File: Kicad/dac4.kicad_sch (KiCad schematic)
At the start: 10 parts

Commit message: Update schematic files to Kicad 6.
Had to fix some symbols which didn't have perfect matches in K6.
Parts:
- renumbered R1501 to R9001, R1502 to R9002, R1503 to R9003, R1504 to R9004, R1505 to R9005, R1506 to R9006, R1507 to R9007, R1508 to R9008, R1509 to R9009, R1510 to R9010
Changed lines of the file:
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@@
   (symbol (lib_id "Device:R") (at 88.9 68.58 0) (unit 1)
     (in_bom yes) (on_board yes)
-    (property "Reference" "R1501" (id 0) (at 90.678 67.4116 0)
+    (property "Reference" "R9001" (id 0) (at 90.678 67.4116 0)
       (effects (font (size 1.27 1.27)) (justify left))
     )
@@
   (symbol (lib_id "Device:R") (at 165.1 68.58 0) (unit 1)
     (in_bom yes) (on_board yes)
-    (property "Reference" "R1508" (id 0) (at 166.878 67.4116 0)
+    (property "Reference" "R9008" (id 0) (at 166.878 67.4116 0)
       (effects (font (size 1.27 1.27)) (justify left))
     )
@@
   (symbol (lib_id "Device:R") (at 101.6 76.2 270) (unit 1)
     (in_bom yes) (on_board yes)
-    (property "Reference" "R1503" (id 0) (at 101.6 78.74 90))
+    (property "Reference" "R9003" (id 0) (at 101.6 78.74 90))
     (property "Value" "12k" (id 1) (at 101.6 81.28 90))
     (property "Footprint" "Resistor_SMD:R_0805_2012Metric_Pad1.20x1.40mm_HandSolder" (id 2) (at 101.6 74.422 90)
@@
   (symbol (lib_id "Device:R") (at 114.3 68.58 0) (unit 1)
     (in_bom yes) (on_board yes)
-    (property "Reference" "R1504" (id 0) (at 116.078 67.4116 0)
+    (property "Reference" "R9004" (id 0) (at 116.078 67.4116 0)
       (effects (font (size 1.27 1.27)) (justify left))
     )
@@
   (symbol (lib_id "Device:R") (at 127 76.2 270) (unit 1)
     (in_bom yes) (on_board yes)
-    (property "Reference" "R1505" (id 0) (at 127 78.74 90))
+    (property "Reference" "R9005" (id 0) (at 127 78.74 90))
     (property "Value" "12k" (id 1) (at 127 81.28 90))
     (property "Footprint" "Resistor_SMD:R_0805_2012Metric_Pad1.20x1.40mm_HandSolder" (id 2) (at 127 74.422 90)
@@
   (symbol (lib_id "Device:R") (at 152.4 76.2 270) (unit 1)
     (in_bom yes) (on_board yes)
-    (property "Reference" "R1507" (id 0) (at 152.4 78.74 90))
+    (property "Reference" "R9007" (id 0) (at 152.4 78.74 90))
     (property "Value" "12k" (id 1) (at 152.4 81.28 90))
     (property "Footprint" "Resistor_SMD:R_0805_2012Metric_Pad1.20x1.40mm_HandSolder" (id 2) (at 152.4 74.422 90)
@@
   (symbol (lib_id "Device:R") (at 177.8 76.2 270) (unit 1)
     (in_bom yes) (on_board yes)
-    (property "Reference" "R1509" (id 0) (at 177.8 78.74 90))
+    (property "Reference" "R9009" (id 0) (at 177.8 78.74 90))
     (property "Value" "12k" (id 1) (at 177.8 81.28 90))
     (property "Footprint" "Resistor_SMD:R_0805_2012Metric_Pad1.20x1.40mm_HandSolder" (id 2) (at 177.8 74.422 90)
@@
   (symbol (lib_id "Device:R") (at 191.77 83.82 0) (unit 1)
     (in_bom yes) (on_board yes)
-    (property "Reference" "R1510" (id 0) (at 193.548 82.6516 0)
+    (property "Reference" "R9010" (id 0) (at 193.548 82.6516 0)
       (effects (font (size 1.27 1.27)) (justify left))
     )
@@
   (symbol (lib_id "power:GND") (at 88.9 91.44 0) (unit 1)
     (in_bom yes) (on_board yes)
-    (property "Reference" "#PWR01501" (id 0) (at 88.9 97.79 0)
+    (property "Reference" "#PWR09001" (id 0) (at 88.9 97.79 0)
       (effects (font (size 1.27 1.27)) hide)
     )
@@
   (symbol (lib_id "power:GND") (at 191.77 91.44 0) (unit 1)
     (in_bom yes) (on_board yes)
-    (property "Reference" "#PWR01502" (id 0) (at 191.77 97.79 0)
+    (property "Reference" "#PWR09002" (id 0) (at 191.77 97.79 0)
       (effects (font (size 1.27 1.27)) hide)
     )
@@
   (symbol (lib_id "Device:R") (at 88.9 83.82 0) (unit 1)
     (in_bom yes) (on_board yes)
-    (property "Reference" "R1502" (id 0) (at 90.678 82.6516 0)
+    (property "Reference" "R9002" (id 0) (at 90.678 82.6516 0)
       (effects (font (size 1.27 1.27)) (justify left))
     )
@@
   (symbol (lib_id "Device:R") (at 139.7 68.58 0) (unit 1)
     (in_bom yes) (on_board yes)
-    (property "Reference" "R1506" (id 0) (at 141.478 67.4116 0)
-      (effects (font (size 1.27 1.27)) (justify left))
-    )
+    (property "Reference" "R9006" (id 0) (at 141.478 67.4116 0)
+      (effects (font (size 1.27 1.27)) (justify left))
+    )

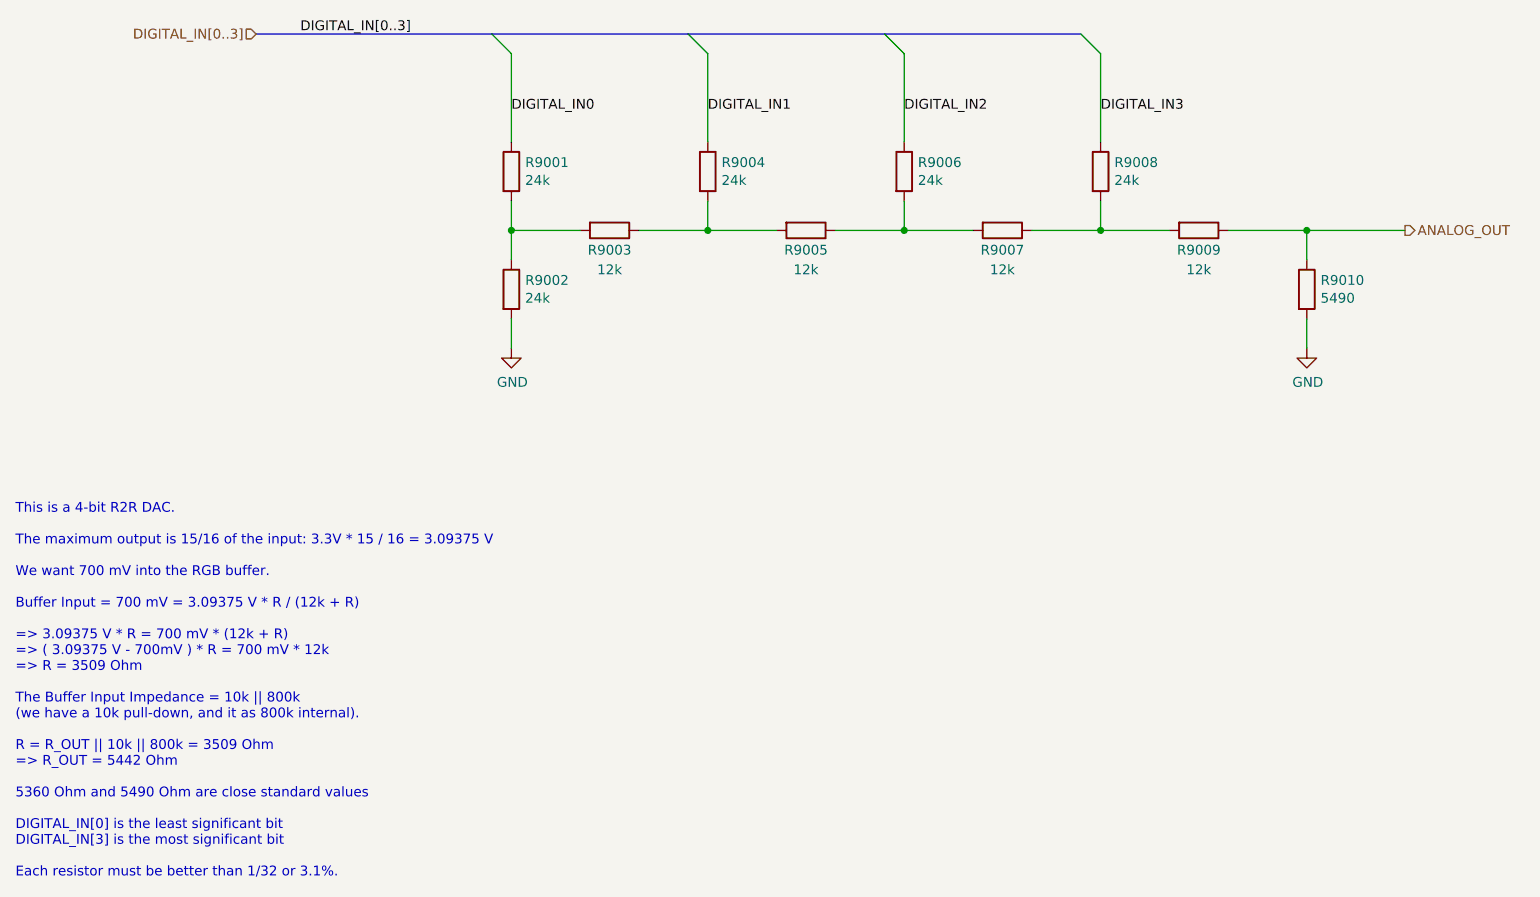
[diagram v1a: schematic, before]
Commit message: Imported sheets from Neotron Pico.
Standardised on +3V3 not +3.3V
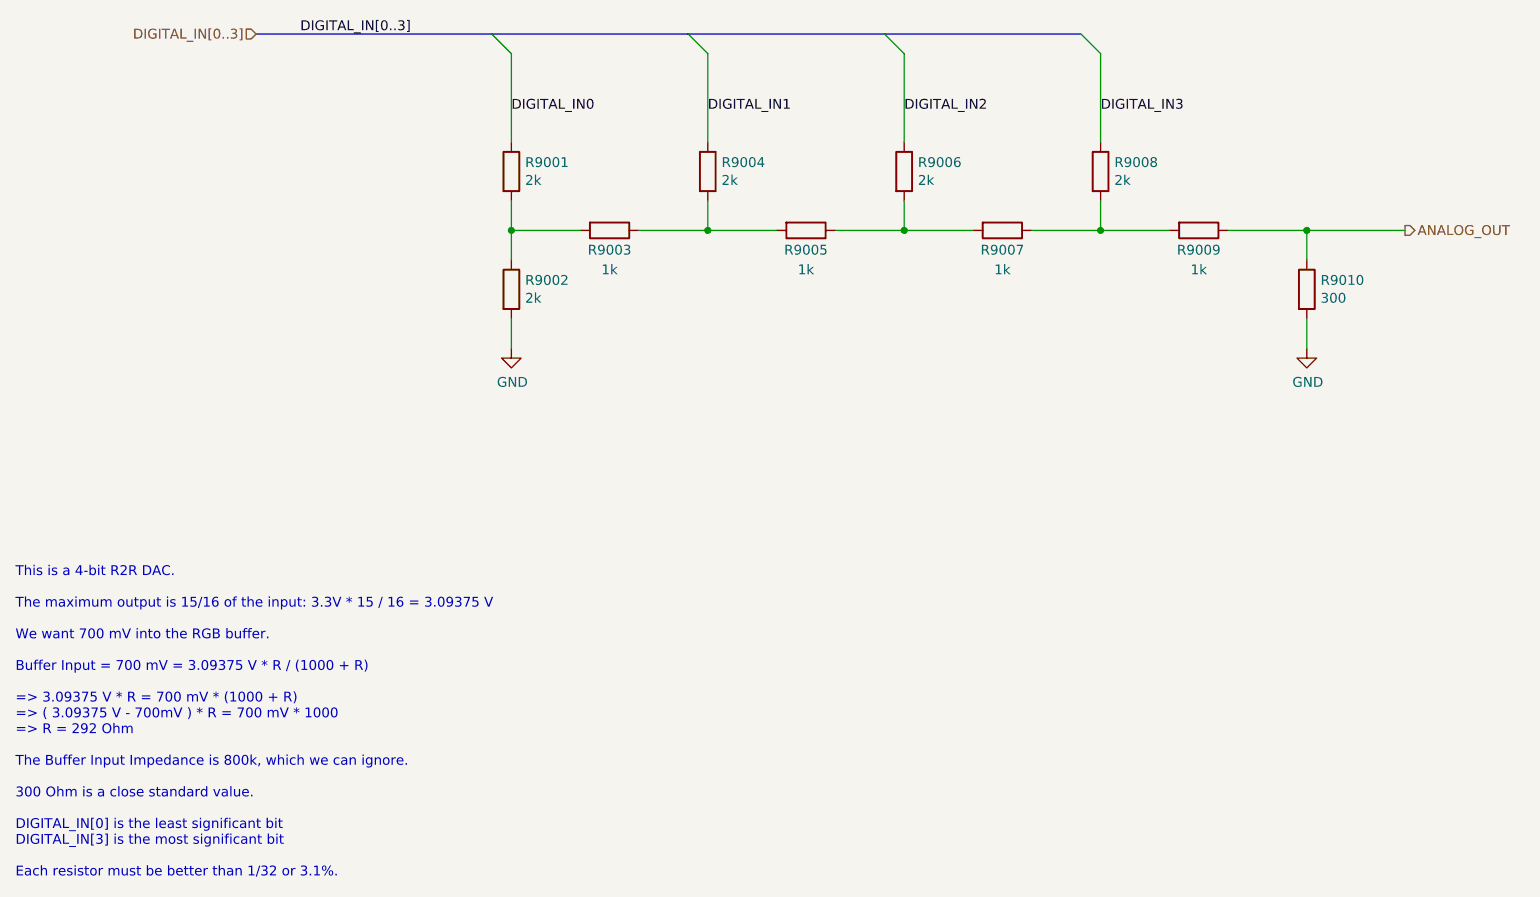
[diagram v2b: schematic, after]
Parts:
- R9001, R9002, R9004, R9006, R9008: value 24k -> 2k; Digikey RNCF0805DTE24K0CT-ND -> (none); JLCPCB Collection (none) -> Basic; LCSC Part# C17575 -> C17604; MPN RMCF0805FT24K0 -> 0805W8F2001T5E; Manufacturer Stackpole -> Uniroyal
- R9003, R9005, R9007, R9009: value 12k -> 1k; Digikey RNCF0805DTE12K0CT-ND -> (none); JLCPCB Collection (none) -> Basic; LCSC Part# C97163 -> C17513; MPN RMCF0805FT12K0 -> 0805W8F1001T5E; Manufacturer Stackpole -> Uniroyal
- R9010: value 5490 -> 300; Digikey RNCF0805DTE5K49CT-ND -> (none); JLCPCB Collection (none) -> Basic; LCSC Part# C79483 -> C17617; MPN RMCF0805FT5K49 -> 0805W8F3000T5E; Manufacturer Stackpole -> Uniroyal
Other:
- note added: "This is a 4-bit R2R DAC. The maximum output is 15/16 of the input: 3.3V * 15 / 16 = 3.09375 V We want 700 mV into the RGB buffer. Buffer Input = 700 mV = 3.09375 V * R / (1000 + R) => 3.09375 V * R = 700 mV * (1000 + R) => ( 3.09375 V - 700mV ) * R = 700 mV * 1000 => R = 292 Ohm The Buffer Input Impedance is 800k, which we can ignore. 300 Ohm is a close standard value. DIGITAL_IN[0] is the least 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"
- note removed: "This is a 4-bit R2R DAC. The maximum output is 15/16 of the input: 3.3V * 15 / 16 = 3.09375 V We want 700 mV into the RGB buffer. Buffer Input = 700 mV = 3.09375 V * R / (12k + R) => 3.09375 V * R = 700 mV * (12k + R) => ( 3.09375 V - 700mV ) * R = 700 mV * 12k => R = 3509 Ohm The Buffer Input Impedance = 10k || 800k (we have a 10k pull-down, and it as 800k internal). R = R_OUT || 10k || 800k = 3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"
- company: https://neotron-compute.github.io/ -> https://neotron-compute.github.io

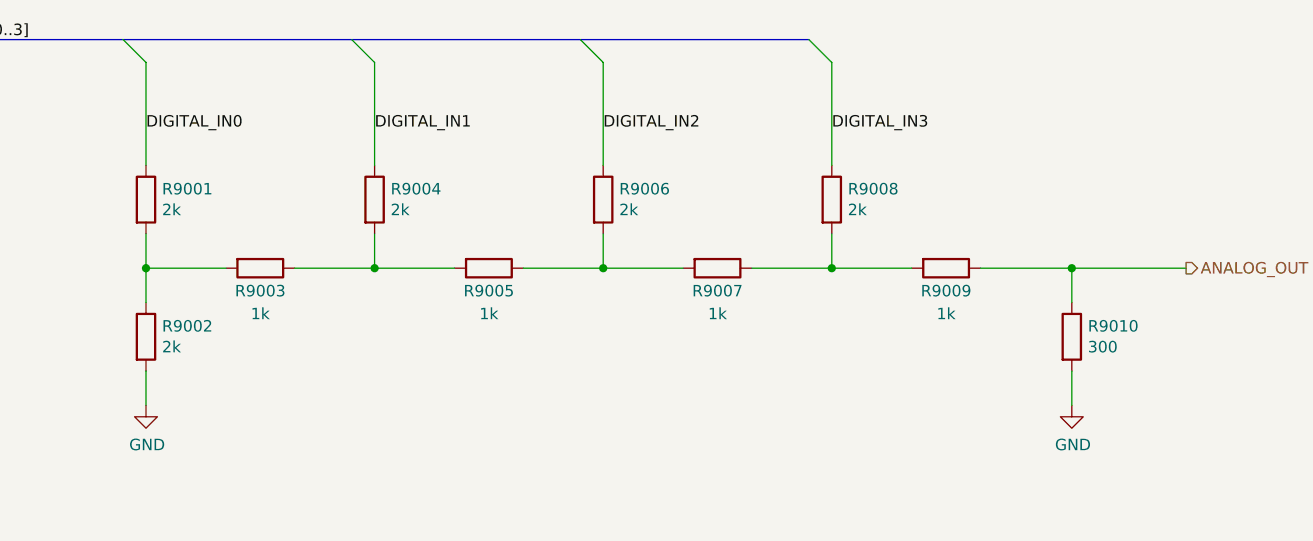
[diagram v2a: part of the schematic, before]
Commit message: Re-imported from Neotron Pico v1.1.
This time I deleted the sheets from the top level and then re-added pointing at the new files. I also reset the PCB dimensions to match the Neotron Pico.

This seems to have done a better job importing footprints.
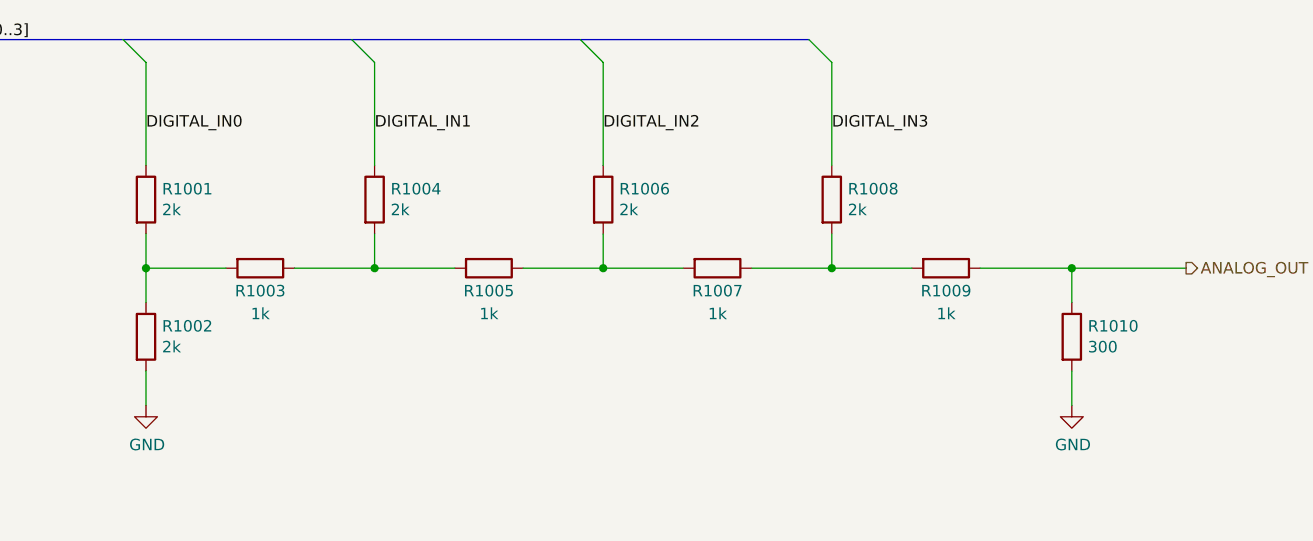
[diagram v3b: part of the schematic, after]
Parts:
- renumbered R9001 to R1001, R9002 to R1002, R9003 to R1003, R9004 to R1004, R9005 to R1005, R9006 to R1006, R9007 to R1007, R9008 to R1008, R9009 to R1009, R9010 to R1010
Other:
- company: https://neotron-compute.github.io -> https://neotron-compute.github.io/
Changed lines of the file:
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@@
     (title "Neotron Common Hardware - 4-bit DAC")
     (date "${date}")
-    (rev "${version}")
-    (company "https://neotron-compute.github.io")
-    (comment 1 "Licensed as CC-BY-SA")
+    (rev "[Uncontrolled]")
+    (company "https://neotron-compute.github.io/")
+    (comment 1 "Licenced as CC BY-SA")
     (comment 2 "Copyright (c) The Neotron Developers, 2022")
   )
@@
   (symbol (lib_id "Device:R") (at 88.9 68.58 0) (unit 1)
     (in_bom yes) (on_board yes)
-    (property "Reference" "R9001" (id 0) (at 90.678 67.4116 0)
+    (property "Reference" "R1001" (id 0) (at 90.678 67.4116 0)
       (effects (font (size 1.27 1.27)) (justify left))
     )
@@
       (effects (font (size 1.27 1.27)) hide)
     )
-    (property "Digikey" "" (id 5) (at 88.9 68.58 0)
+    (property "Digikey" "~" (id 5) (at 88.9 68.58 0)
       (effects (font (size 1.27 1.27)) hide)
     )
@@
       (effects (font (size 1.27 1.27)) hide)
     )
-    (property "Mouser" "" (id 11) (at 88.9 68.58 0)
+    (property "Mouser" "~" (id 11) (at 88.9 68.58 0)
       (effects (font (size 1.27 1.27)) hide)
     )
@@
   (symbol (lib_id "Device:R") (at 165.1 68.58 0) (unit 1)
     (in_bom yes) (on_board yes)
-    (property "Reference" "R9008" (id 0) (at 166.878 67.4116 0)
+    (property "Reference" "R1008" (id 0) (at 166.878 67.4116 0)
       (effects (font (size 1.27 1.27)) (justify left))
     )
@@
       (effects (font (size 1.27 1.27)) hide)
     )
-    (property "Digikey" "" (id 5) (at 165.1 68.58 0)
+    (property "Digikey" "~" (id 5) (at 165.1 68.58 0)
       (effects (font (size 1.27 1.27)) hide)
     )
@@
       (effects (font (size 1.27 1.27)) hide)
     )
-    (property "Mouser" "" (id 11) (at 165.1 68.58 0)
+    (property "Mouser" "~" (id 11) (at 165.1 68.58 0)
       (effects (font (size 1.27 1.27)) hide)
     )
@@
   (symbol (lib_id "Device:R") (at 101.6 76.2 270) (unit 1)
     (in_bom yes) (on_board yes)
-    (property "Reference" "R9003" (id 0) (at 101.6 78.74 90))
+    (property "Reference" "R1003" (id 0) (at 101.6 78.74 90))
     (property "Value" "1k" (id 1) (at 101.6 81.28 90))
     (property "Footprint" "Resistor_SMD:R_0805_2012Metric_Pad1.20x1.40mm_HandSolder" (id 2) (at 101.6 74.422 90)
@@
   (symbol (lib_id "Device:R") (at 114.3 68.58 0) (unit 1)
     (in_bom yes) (on_board yes)
-    (property "Reference" "R9004" (id 0) (at 116.078 67.4116 0)
+    (property "Reference" "R1004" (id 0) (at 116.078 67.4116 0)
       (effects (font (size 1.27 1.27)) (justify left))
     )
@@
       (effects (font (size 1.27 1.27)) hide)
     )
-    (property "Digikey" "" (id 5) (at 114.3 68.58 0)
+    (property "Digikey" "~" (id 5) (at 114.3 68.58 0)
       (effects (font (size 1.27 1.27)) hide)
     )
@@
       (effects (font (size 1.27 1.27)) hide)
     )
-    (property "Mouser" "" (id 11) (at 114.3 68.58 0)
+    (property "Mouser" "~" (id 11) (at 114.3 68.58 0)
       (effects (font (size 1.27 1.27)) hide)
     )
@@
   (symbol (lib_id "Device:R") (at 127 76.2 270) (unit 1)
     (in_bom yes) (on_board yes)
-    (property "Reference" "R9005" (id 0) (at 127 78.74 90))
+    (property "Reference" "R1005" (id 0) (at 127 78.74 90))
     (property "Value" "1k" (id 1) (at 127 81.28 90))
     (property "Footprint" "Resistor_SMD:R_0805_2012Metric_Pad1.20x1.40mm_HandSolder" (id 2) (at 127 74.422 90)
@@
   (symbol (lib_id "Device:R") (at 152.4 76.2 270) (unit 1)
     (in_bom yes) (on_board yes)
-    (property "Reference" "R9007" (id 0) (at 152.4 78.74 90))
+    (property "Reference" "R1007" (id 0) (at 152.4 78.74 90))
     (property "Value" "1k" (id 1) (at 152.4 81.28 90))
     (property "Footprint" "Resistor_SMD:R_0805_2012Metric_Pad1.20x1.40mm_HandSolder" (id 2) (at 152.4 74.422 90)
@@
   (symbol (lib_id "Device:R") (at 177.8 76.2 270) (unit 1)
     (in_bom yes) (on_board yes)
-    (property "Reference" "R9009" (id 0) (at 177.8 78.74 90))
+    (property "Reference" "R1009" (id 0) (at 177.8 78.74 90))
     (property "Value" "1k" (id 1) (at 177.8 81.28 90))
     (property "Footprint" "Resistor_SMD:R_0805_2012Metric_Pad1.20x1.40mm_HandSolder" (id 2) (at 177.8 74.422 90)
@@
   (symbol (lib_id "Device:R") (at 191.77 83.82 0) (unit 1)
     (in_bom yes) (on_board yes)
-    (property "Reference" "R9010" (id 0) (at 193.548 82.6516 0)
+    (property "Reference" "R1010" (id 0) (at 193.548 82.6516 0)
       (effects (font (size 1.27 1.27)) (justify left))
     )
@@
   (symbol (lib_id "power:GND") (at 88.9 91.44 0) (unit 1)
     (in_bom yes) (on_board yes)
-    (property "Reference" "#PWR09001" (id 0) (at 88.9 97.79 0)
+    (property "Reference" "#PWR01001" (id 0) (at 88.9 97.79 0)
       (effects (font (size 1.27 1.27)) hide)
     )
@@
   (symbol (lib_id "power:GND") (at 191.77 91.44 0) (unit 1)
     (in_bom yes) (on_board yes)
-    (property "Reference" "#PWR09002" (id 0) (at 191.77 97.79 0)
+    (property "Reference" "#PWR01002" (id 0) (at 191.77 97.79 0)
       (effects (font (size 1.27 1.27)) hide)
     )
@@
   (symbol (lib_id "Device:R") (at 88.9 83.82 0) (unit 1)
     (in_bom yes) (on_board yes)
-    (property "Reference" "R9002" (id 0) (at 90.678 82.6516 0)
+    (property "Reference" "R1002" (id 0) (at 90.678 82.6516 0)
       (effects (font (size 1.27 1.27)) (justify left))
     )
@@
       (effects (font (size 1.27 1.27)) hide)
     )
-    (property "Digikey" "" (id 5) (at 88.9 83.82 0)
+    (property "Digikey" "~" (id 5) (at 88.9 83.82 0)
       (effects (font (size 1.27 1.27)) hide)
     )
@@
       (effects (font (size 1.27 1.27)) hide)
     )
-    (property "Mouser" "" (id 11) (at 88.9 83.82 0)
+    (property "Mouser" "~" (id 11) (at 88.9 83.82 0)
       (effects (font (size 1.27 1.27)) hide)
     )
@@
   (symbol (lib_id "Device:R") (at 139.7 68.58 0) (unit 1)
     (in_bom yes) (on_board yes)
-    (property "Reference" "R9006" (id 0) (at 141.478 67.4116 0)
+    (property "Reference" "R1006" (id 0) (at 141.478 67.4116 0)
       (effects (font (size 1.27 1.27)) (justify left))
     )
@@
       (effects (font (size 1.27 1.27)) hide)
     )
-    (property "Digikey" "" (id 5) (at 139.7 68.58 0)
+    (property "Digikey" "~" (id 5) (at 139.7 68.58 0)
       (effects (font (size 1.27 1.27)) hide)
     )
@@
       (effects (font (size 1.27 1.27)) hide)
     )
-    (property "Mouser" "" (id 11) (at 139.7 68.58 0)
-      (effects (font (size 1.27 1.27)) hide)
-    )
+    (property "Mouser" "~" (id 11) (at 139.7 68.58 0)
+      (effects (font (size 1.27 1.27)) hide)
+    )
